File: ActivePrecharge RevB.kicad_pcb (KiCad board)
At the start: 2 copper layers, 98.4 x 58.9 mm, 93 parts, among them IC1 AMC1350DWVR, IC2 AMC1350DWVR, IC3 ZXRE160AET5TA, J1 HVConnector, J2 ExportConnector, J3 PrechargeContactor, J4 MainContactor, U1 LT1963AEST-3.3#TRPBF, U2 TLV9001IDBVR, U3 TLV9001IDBVR

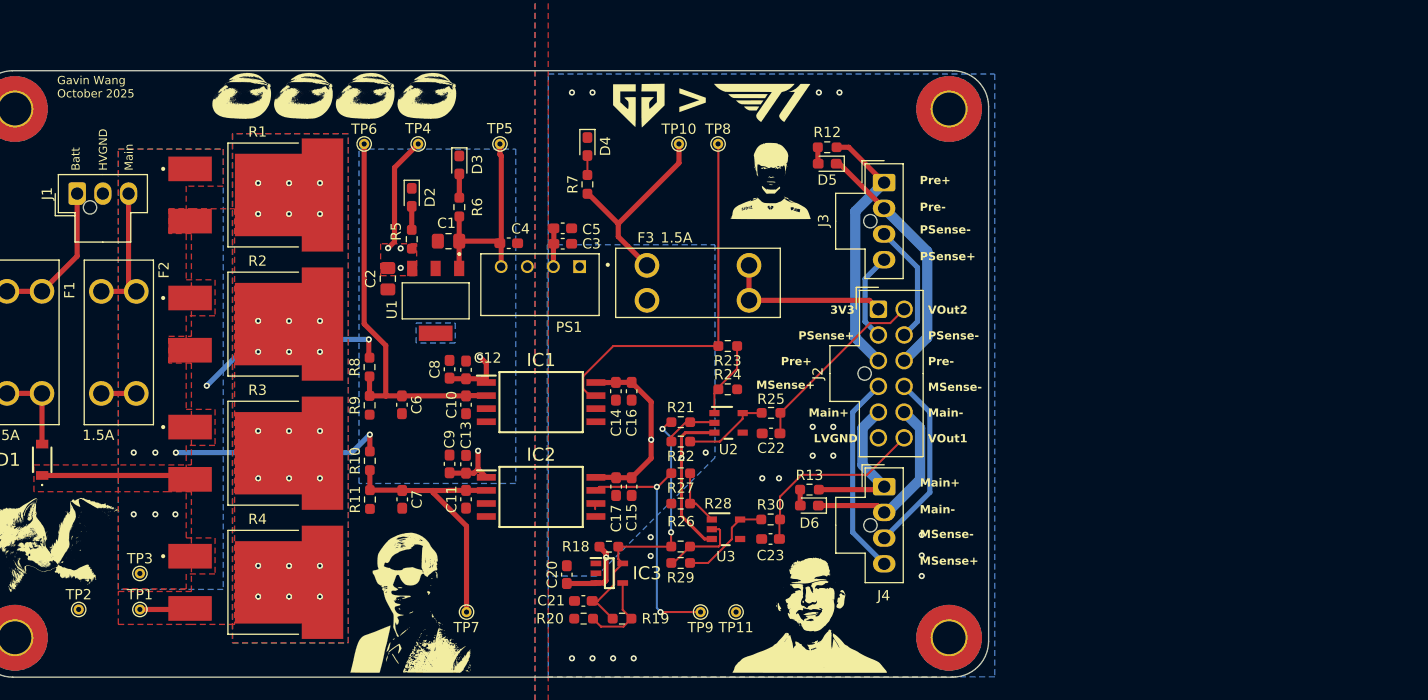
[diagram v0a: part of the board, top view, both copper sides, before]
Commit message: Removed the 0.8V Reference circuit, changed the opamp, and changed the testpoints to make testing easier. Not sure how the connector is meant to be set up though
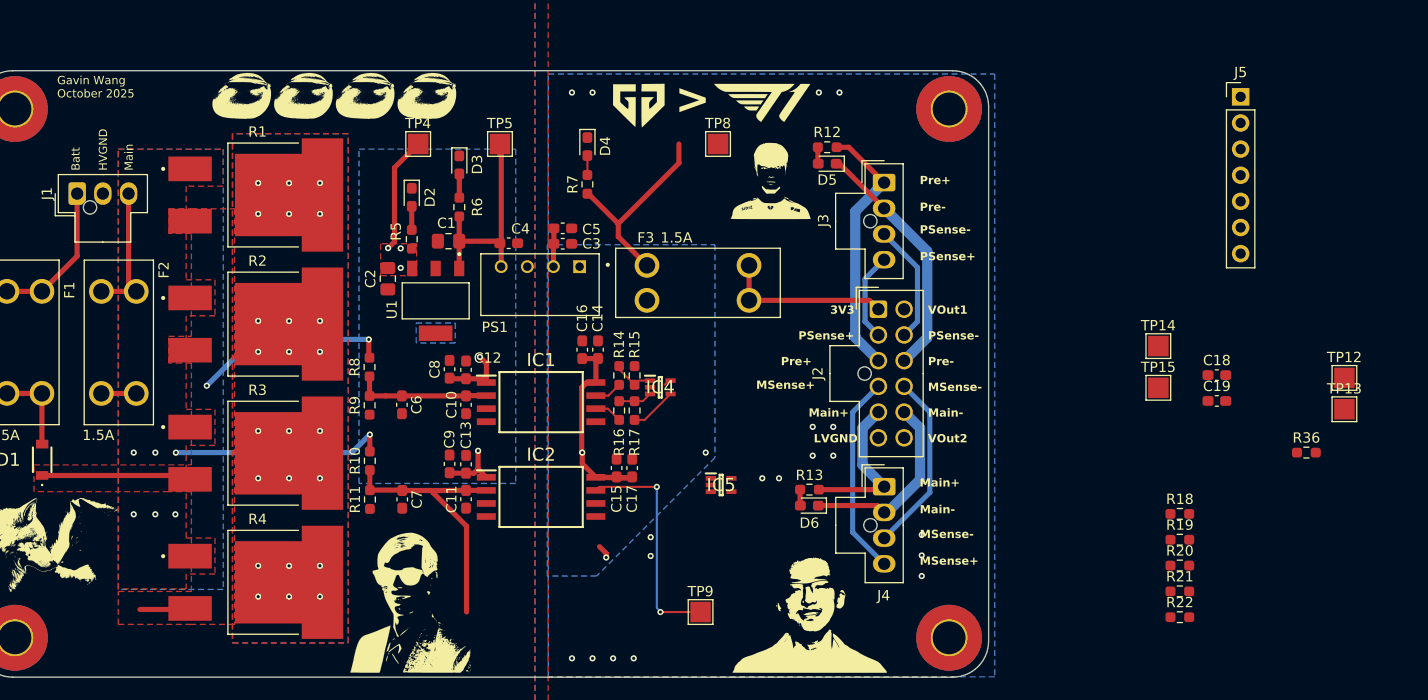
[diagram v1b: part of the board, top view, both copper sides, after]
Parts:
- removed C20: 100nF, Capacitor_SMD:C_0603_1608Metric_Pad1.08x0.95mm_HandSolder
- removed C21: 0.47uF, Capacitor_SMD:C_0603_1608Metric_Pad1.08x0.95mm_HandSolder
- removed C22, C23: 10nF, Capacitor_SMD:C_0603_1608Metric_Pad1.08x0.95mm_HandSolder
- removed IC3: ZXRE160AET5TA, ActivePrecharge-RevB:SOT95P280X100-5N
- removed R23, R26, R27: 2.49k, Resistor_SMD:R_0603_1608Metric_Pad0.98x0.95mm_HandSolder
- removed R24, R28, R29: 15k, Resistor_SMD:R_0603_1608Metric_Pad0.98x0.95mm_HandSolder
- removed R25, R30: 10, Resistor_SMD:R_0603_1608Metric_Pad0.98x0.95mm_HandSolder
- removed TP1: HV+, TestPoint:TestPoint_THTPad_D1.0mm_Drill0.5mm
- removed TP10: 3V3, TestPoint:TestPoint_THTPad_D1.0mm_Drill0.5mm
- removed TP11: LVGND, TestPoint:TestPoint_THTPad_D1.0mm_Drill0.5mm
- removed TP2: HVGND, TestPoint:TestPoint_THTPad_D1.0mm_Drill0.5mm
- removed TP3: HV-, TestPoint:TestPoint_THTPad_D1.0mm_Drill0.5mm
- removed TP6: Vin1, TestPoint:TestPoint_THTPad_D1.0mm_Drill0.5mm
- removed TP7: Vin2, TestPoint:TestPoint_THTPad_D1.0mm_Drill0.5mm
- removed U2, U3: TLV9001IDBVR, ActivePrecharge-RevB:DBV0005A_N
- added C18: 10nF, Capacitor_SMD:C_0603_1608Metric_Pad1.08x0.95mm_HandSolder, F.Cu at (220.7, 89.5)
- added C19: 10nF, Capacitor_SMD:C_0603_1608Metric_Pad1.08x0.95mm_HandSolder, F.Cu at (220.7, 92.0)
- added IC4: MCP6496UT-E_LT, ActivePrecharge-RevB:SOT65P210X110-5N, F.Cu at (166.6, 90.7)
- added IC5: MCP6496UT-E_LT, ActivePrecharge-RevB:SOT65P210X110-5N, F.Cu at (172.5, 100.2)
- added J5: Conn_01x07_Pin, Connector_PinHeader_2.54mm:PinHeader_1x07_P2.54mm_Vertical, F.Cu at (223.0, 62.4)
- added R14: 20k, Resistor_SMD:R_0603_1608Metric_Pad0.98x0.95mm_HandSolder, F.Cu at (162.6, 89.5)
- added R15: 50k, Resistor_SMD:R_0603_1608Metric_Pad0.98x0.95mm_HandSolder, F.Cu at (164.1, 89.5)
- added R16: 20k, Resistor_SMD:R_0603_1608Metric_Pad0.98x0.95mm_HandSolder, F.Cu at (162.6, 92.9)
- added R17: 50k, Resistor_SMD:R_0603_1608Metric_Pad0.98x0.95mm_HandSolder, F.Cu at (164.1, 92.9)
- added R36: 23, Resistor_SMD:R_0603_1608Metric_Pad0.98x0.95mm_HandSolder, F.Cu at (229.4, 97.0)
- added TP12: V1-, TestPoint:TestPoint_Pad_2.0x2.0mm, F.Cu at (233.1, 89.7)
- added TP13: V2-, TestPoint:TestPoint_Pad_2.0x2.0mm, F.Cu at (233.1, 92.8)
- added TP14: VOut1, TestPoint:TestPoint_Pad_2.0x2.0mm, F.Cu at (215.0, 86.7)
- added TP15: VOut2, TestPoint:TestPoint_Pad_2.0x2.0mm, F.Cu at (215.0, 90.7)
- R18: value 1k -> 10
- R19: value 5.1k -> 20k
- R20, R22: value 15k -> 50k
- R21: value 2.49k -> 20k
- TP4, TP5: footprint TestPoint:TestPoint_THTPad_D1.0mm_Drill0.5mm -> TestPoint:TestPoint_Pad_2.0x2.0mm
- TP8: value V1 -> V1+; footprint TestPoint:TestPoint_THTPad_D1.0mm_Drill0.5mm -> TestPoint:TestPoint_Pad_2.0x2.0mm
- TP9: value V2 -> V2+; footprint TestPoint:TestPoint_THTPad_D1.0mm_Drill0.5mm -> TestPoint:TestPoint_Pad_2.0x2.0mm
- moved R20 58.2 mm to (217.1, 108.0), turned to 0 degrees
- moved R18 55.6 mm to (217.1, 103.0)
- moved R19 54.8 mm to (217.1, 105.5), turned to 0 degrees
- moved R22 51.4 mm to (217.1, 113.0), turned to 0 degrees
- moved R21 51.2 mm to (217.1, 110.5)
- moved C16 6.27 mm to (159.0, 87.0), turned to 90 degrees
- moved C14 4.40 mm to (160.5, 87.0), turned to 90 degrees
- moved C17 2.39 mm to (163.8, 98.5), turned to 90 degrees
- moved C15 2.32 mm to (162.3, 98.5), turned to 90 degrees
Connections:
- net /Voltage_Sense/V1 renamed /Voltage_Sense/V1+
- IC1 pad 6: LVGND -> /Voltage_Sense/V1-
- IC2 pad 6: LVGND -> /Voltage_Sense/V2-
- IC2 pad 7: /Voltage_Sense/V2 -> /Voltage_Sense/V2+
- R18 pad 1: 3V3 -> /VOut1
- R18 pad 2: REG_0V8 -> Net-(IC4-VOUT)
- R19 pad 1: Net-(IC3-FB) -> Net-(IC5-VIN+)
- R19 pad 2: REG_0V8 -> /Voltage_Sense/V2+
- R20 pad 1: Net-(IC3-FB) -> LVGND
- R20 pad 2: LVGND -> Net-(IC5-VIN+)
- R21 pad 1: REG_0V8 -> Net-(IC5-VIN-)
- R21 pad 2: Net-(U2--) -> /Voltage_Sense/V2-
- R22 pad 2: Net-(U2--) -> Net-(IC5-VIN-)
- TP9 pad 1: /Voltage_Sense/V2 -> /Voltage_Sense/V2+
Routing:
- net /Voltage_Sense/V1+: track 36.7 -> 2.70 mm
- net REG_0V8: track 27.8 -> 0.00 mm, vias 2 -> 0
- net /Voltage_Sense/Vin1: track 38.6 -> 13.3 mm
- net /Voltage_Sense/V2: track 24.2 -> 0.00 mm, vias 2 -> 0
- net /Voltage_Sense/V2+: track 0.00 -> 22.3 mm, vias 0 -> 2
- net 3V3: track 64.9 -> 45.9 mm, vias 3 -> 2
- net /VOut2: track 18.6 -> 0.00 mm
- net /VOut1: track 18.1 -> 0.00 mm
- net Net-(R29-Pad1): track 9.33 -> 0.00 mm
- net Net-(IC5-VOUT): track 8.43 -> 0.00 mm
- net Net-(IC3-FB): track 8.30 -> 0.00 mm
- net Net-(U3--): track 7.75 -> 0.00 mm
- net Net-(U2-+): track 7.44 -> 0.00 mm
- net Net-(U3-+): track 5.70 -> 0.00 mm
- net Net-(U2--): track 5.27 -> 0.00 mm
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
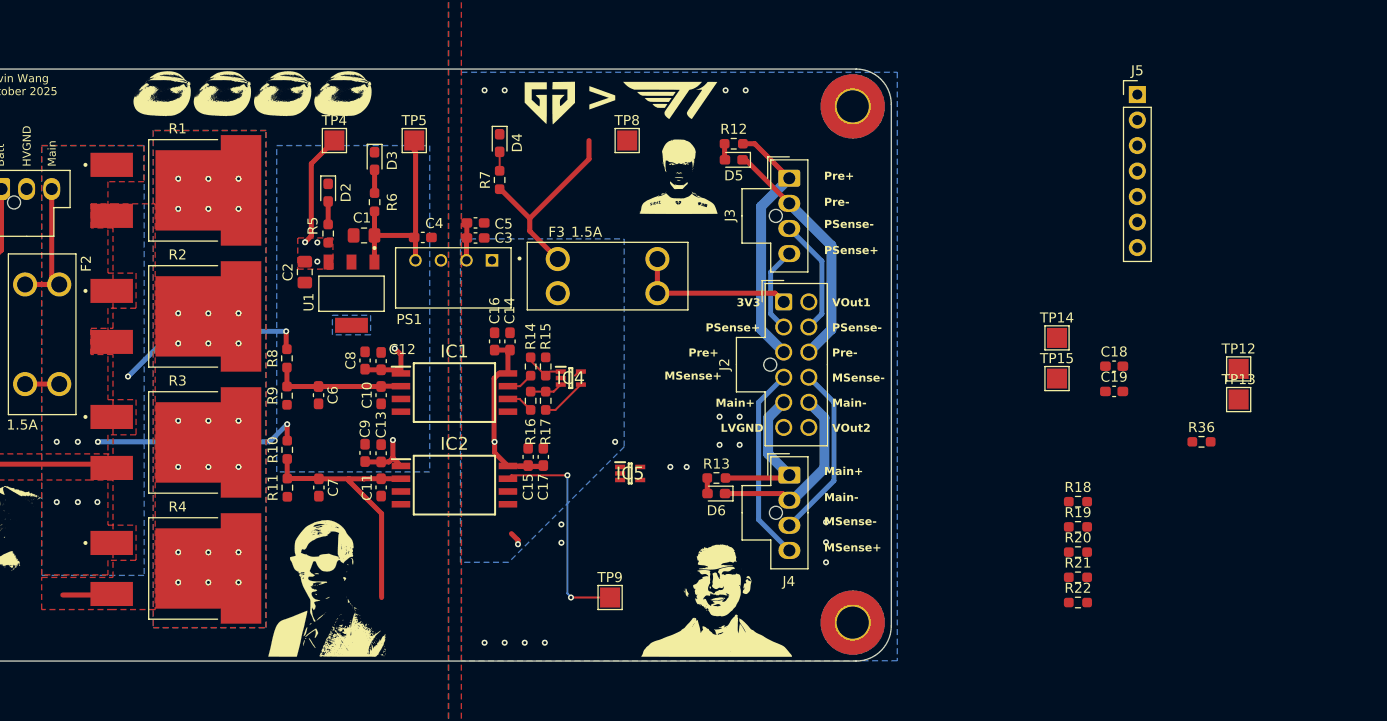
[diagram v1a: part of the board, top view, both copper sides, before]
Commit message: Changed opamp to the TLV9002QDRQ1, separated the pin test points, changed 24V LED resitors to 10k (I don't remember what resistance you guys said), made 2 hierarchical sheets that are linked copies, grouped the calculation for easy reading, and I forgot what other math you wanted me to add that I didn't show.
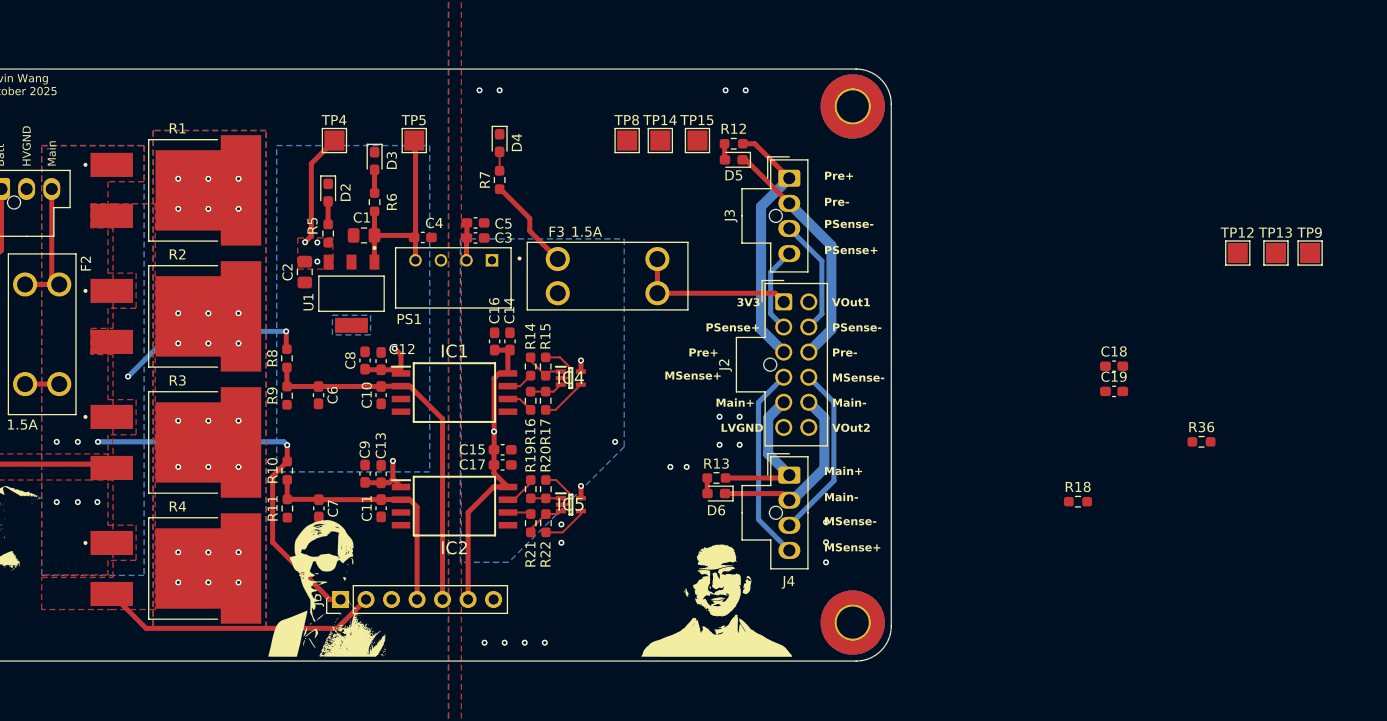
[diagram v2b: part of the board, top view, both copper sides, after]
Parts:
- removed the G*** at (164.5, 63.0)
- removed the G*** at (177.0, 70.6)
- removed the G*** at (176.5, 63.0)
- removed the G*** at (144.0, 62.6)
- removed the G*** at (138.0, 62.6)
- removed the G*** at (126.0, 62.6)
- removed the G*** at (132.0, 62.6)
- moved J5 93.9 mm to (143.7, 112.7), turned to 90 degrees
- moved TP9 77.7 mm to (240.2, 78.2)
- moved R21 54.8 mm to (162.6, 105.1), turned to 90 degrees
- moved R19 54.6 mm to (162.6, 101.7), turned to 90 degrees
- moved R22 53.6 mm to (164.1, 105.1), turned to 90 degrees
- moved R20 53.4 mm to (164.1, 101.7), turned to -90 degrees
- moved TP14 44.1 mm to (175.5, 67.0)
- moved TP15 42.9 mm to (179.2, 67.0)
- moved TP13 15.1 mm to (236.8, 78.2)
- moved TP12 11.5 mm to (233.0, 78.2)
- moved IC5 6.66 mm to (166.6, 103.2)
- moved C17 4.13 mm to (159.8, 99.3), turned to 0 degrees
- moved C15 2.64 mm to (159.8, 97.8), turned to 0 degrees
- moved IC2 2.09 mm to (155.0, 103.4)
- moved C11 2.08 mm to (147.7, 103.6)
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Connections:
- J5 pad 1: HVGND -> HV-
- J5 pad 2: HV- -> HV+
- J5 pad 3: HV+ -> HVGND
- J5 pad 4: /Voltage_Sense/Vin1 -> /Voltage_Sense/Vin2
- J5 pad 5: /Voltage_Sense/Vin2 -> /Voltage_Sense/Vin1
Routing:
- net /Voltage_Sense/Vin1: track 13.3 -> 36.7 mm
- net HV+: track 38.9 -> 62.1 mm
- net /Voltage_Sense/V2+: track 22.3 -> 3.26 mm, vias 2 -> 0
- net HV-: track 25.6 -> 42.7 mm
- net LVGND: track 0.00 -> 9.31 mm
- net Net-(IC5-VOUT): track 0.00 -> 4.54 mm
- net Net-(IC5-VIN-): track 0.00 -> 4.06 mm
- net Net-(IC5-VIN+): track 0.00 -> 3.01 mm
- net /Voltage_Sense/V2-: track 0.00 -> 2.34 mm
- net /Voltage_Sense/Vin2: track 26.4 -> 24.4 mm
- net 3V3: track 45.9 -> 46.1 mm, vias 2 -> 3
- removed copper zone on B.Cu, net LVGND
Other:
- board text removed: ">"
